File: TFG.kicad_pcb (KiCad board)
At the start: 4 copper layers, 119.9 x 80 mm, 35 parts, among them J1 Voltaje Input, J2 IDC-header, U2 LM2596, U3 ESP-WROOM-32, U4 LM339N

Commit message: update sq
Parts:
- removed U3: ESP-WROOM-32, NMDA-lib:MODULE_ESP32_DEVKIT_V1
- added U1: ESP32-DEVKIT-V1, NMDA-lib:MODULE_ESP32_DEVKIT_V1, F.Cu at (43.4, 76.5)
- D1, D2, D3: value 1N4007 -> 2N3896
- R13, R14, R15: value 22k -> 33k
- moved J2 10.7 mm to (124.5, 29.5), turned to 0 degrees
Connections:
- J2 pad 3: TUBE3 -> TUBE1
- J2 pad 7: TUBE1 -> TUBE3
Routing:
- net PULSE_IN_CH01: track 64.4 -> 130.0 mm
- net I2C_SCL: track 36.6 -> 84.5 mm
- net PULSE_IN_CH02: track 127.7 -> 88.3 mm
- net PULSE_IN_CH03: track 118.3 -> 90.5 mm
- net 12V: track 54.1 -> 81.6 mm
- net I2C_SDA: track 42.9 -> 65.9 mm
- net TUBE3: track 32.3 -> 35.5 mm
- net GND: track 77.4 -> 74.7 mm
- net TUBE1: track 36.8 -> 39.4 mm
- net TUBE2: track 30.2 -> 32.1 mm
- net 3.3V: track 272.2 -> 270.4 mm
- net LM1+: track 59.5 -> 61.0 mm

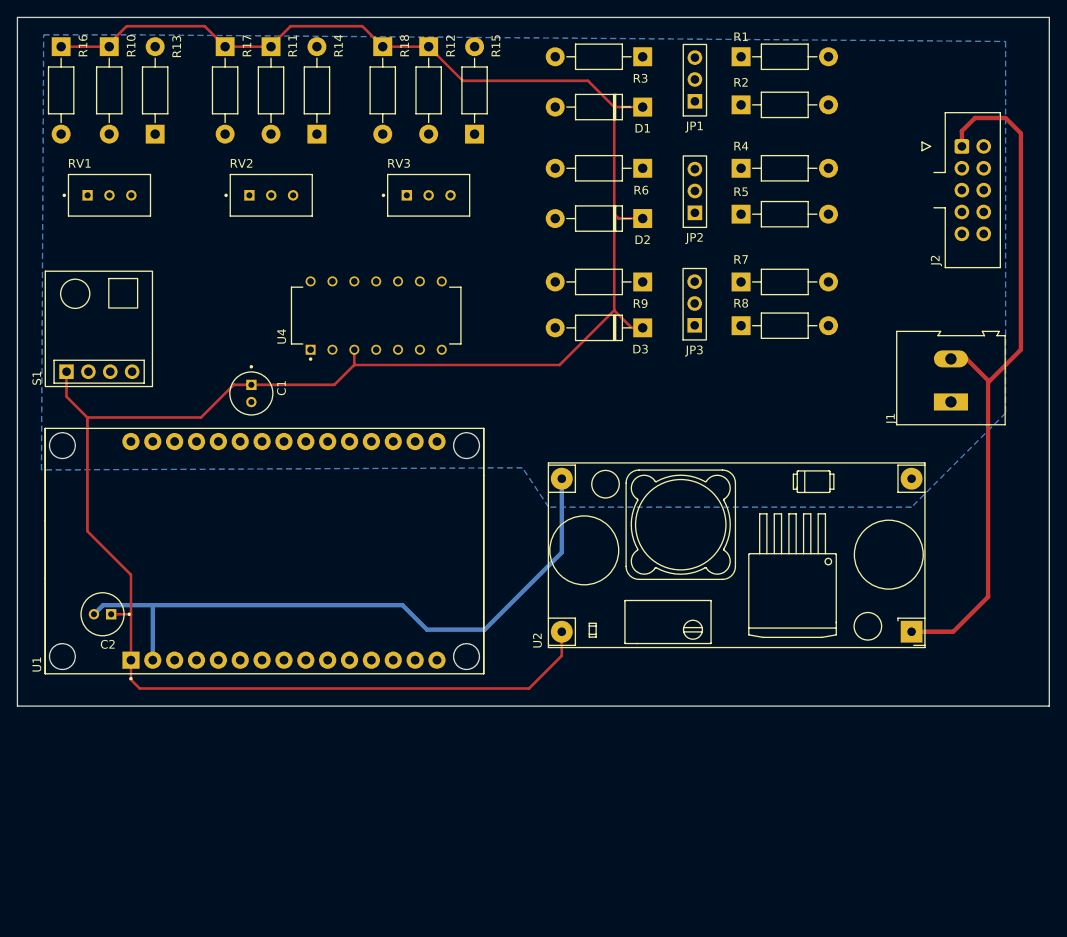
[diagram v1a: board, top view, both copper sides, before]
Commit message: Update PCB 95x95mm
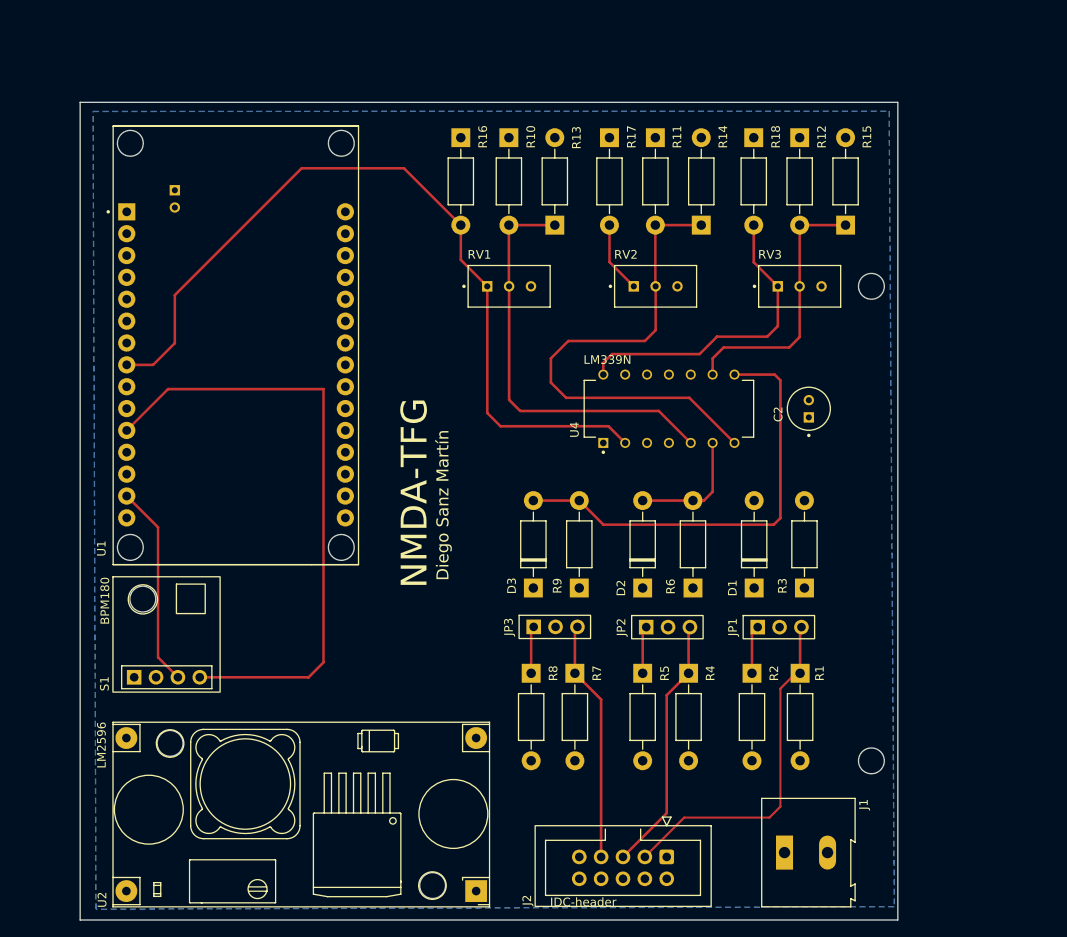
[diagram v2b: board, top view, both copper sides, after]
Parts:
- added ?: , , F.Cu at (114.0, 100.8)
- added ?: , , F.Cu at (29.3, 82.1)
- added ?: , , F.Cu at (114.0, 45.7)
- added ?: , , F.Cu at (63.0, 115.3)
- added ?: , , F.Cu at (32.5, 98.8)
- C1: moved to B.Cu
- moved J2 89.4 mm to (90.2, 112.0), turned to -90 degrees
- moved C2 85.5 mm to (106.7, 59.9), turned to 90 degrees
- moved R1 72.0 mm to (105.7, 90.7), turned to -90 degrees
- moved R2 66.1 mm to (100.1, 90.7), turned to -90 degrees
- moved R3 64.5 mm to (106.2, 80.8), turned to 90 degrees
- moved JP1 64.0 mm to (103.1, 85.1), turned to 0 degrees
- moved R4 59.0 mm to (92.7, 90.7), turned to -90 degrees
- moved U2 58.9 mm to (68.0, 116.0)
- moved D1 57.4 mm to (100.3, 80.8), turned to 90 degrees
- moved J1 55.8 mm to (103.9, 111.5), turned to 0 degrees
- moved R5 54.6 mm to (87.4, 90.7), turned to -90 degrees
- moved JP2 50.4 mm to (90.2, 85.1), turned to 0 degrees
- moved R7 49.4 mm to (79.5, 90.7), turned to -90 degrees
- moved R6 49.1 mm to (93.2, 80.8), turned to 90 degrees
- moved R16 47.6 mm to (66.2, 28.4)
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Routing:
- net 3.3V: track 270.4 -> 0.00 mm
- net 12V: track 81.6 -> 0.00 mm
- net GND: track 74.7 -> 0.00 mm
- net I2C_SCL: track 84.5 -> 23.5 mm
- net PULSE_IN_CH01: track 130.0 -> 94.8 mm
- net LM3-: track 18.5 -> 51.8 mm
- net LM2-: track 45.2 -> 14.2 mm
- net PULSE_IN_CH03: track 90.5 -> 119.3 mm
- net LM1-: track 48.8 -> 21.4 mm
- net PULSE_IN_CH02: track 88.3 -> 67.8 mm
- net LM1+: track 61.0 -> 48.8 mm
- net LM2+: track 47.1 -> 58.1 mm
- net LM3+: track 22.9 -> 31.4 mm
- net TUBE3: track 35.5 -> 28.1 mm
- net I2C_SDA: track 65.9 -> 71.7 mm
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- added copper zone on In2.Cu, net 12V
- added copper zone on In2.Cu, net 3.3V
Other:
- board size 119.9 x 80 mm -> 95 x 95 mm
- board text added: "Diego Sanz Martín"
- board text added: "NMDA-TFG"
